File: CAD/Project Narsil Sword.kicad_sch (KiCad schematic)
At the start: 7 parts, among them SW1 SW_SPDT, U1 BAT-HLD-006-SMT, X1 Badgelife_sao_connector_v169b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, X2 Badgelife_sao_connector_v169b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, X3 Badgelife_sao_connector_v169b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, X4 Badgelife_sao_connector_v169b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, X5 Badgelife_sao_connector_v169b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

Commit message: creating schematic
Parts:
- U1: footprint BadgePirates:BatteryHolder_LINX_BAT-HLD-012-SMT -> BadgePirates:BatteryHolder_MPD_BC2003_1x2032
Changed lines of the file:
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@@
       (effects (font (size 1.27 1.27)) (justify left))
     )
-    (property "Footprint" "BadgePirates:BatteryHolder_LINX_BAT-HLD-012-SMT" (id 2) (at 106.68 85.09 0)
+    (property "Footprint" "BadgePirates:BatteryHolder_MPD_BC2003_1x2032" (id 2) (at 106.68 85.09 0)
       (effects (font (size 1.27 1.27)) (justify left) hide)
     )
@@
     )
     (path "/1e97e274-03d3-49f2-965f-f4108456c327"
-      (reference "U1") (unit 1) (value "BAT-HLD-006-SMT") (footprint "BadgePirates:BatteryHolder_LINX_BAT-HLD-012-SMT")
+      (reference "U1") (unit 1) (value "BAT-HLD-006-SMT") (footprint "BadgePirates:BatteryHolder_MPD_BC2003_1x2032")
     )
     (path "/06e1571b-569f-4df7-9572-da619078c70c"

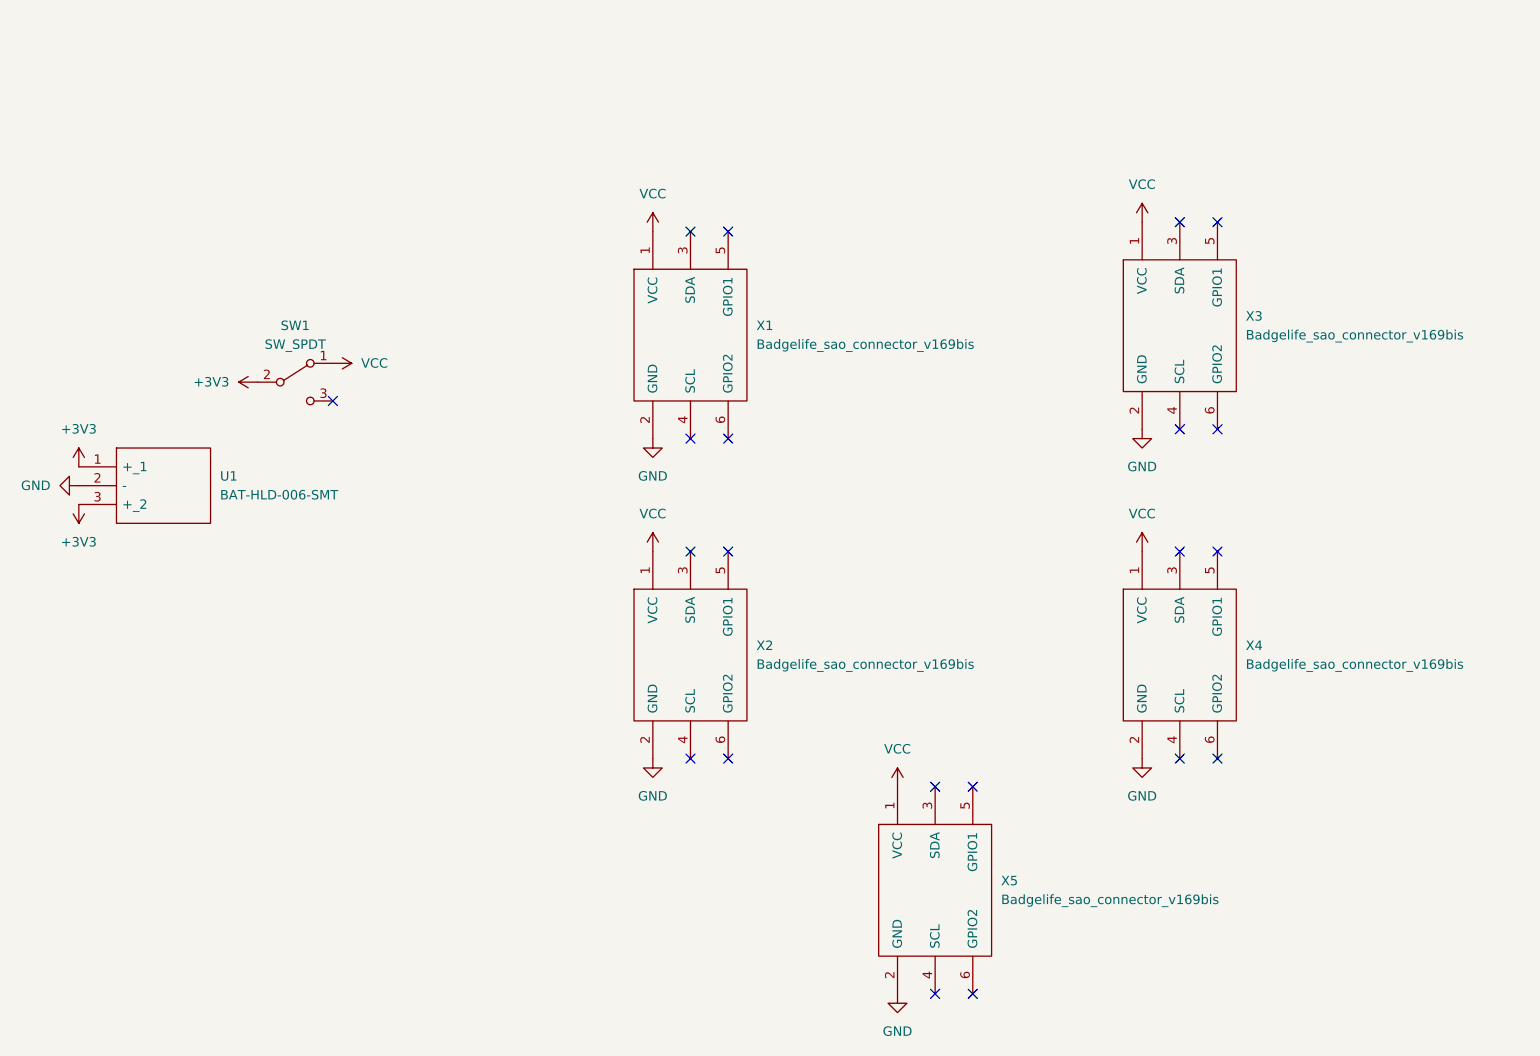
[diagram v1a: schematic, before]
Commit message: update Battery Footprint
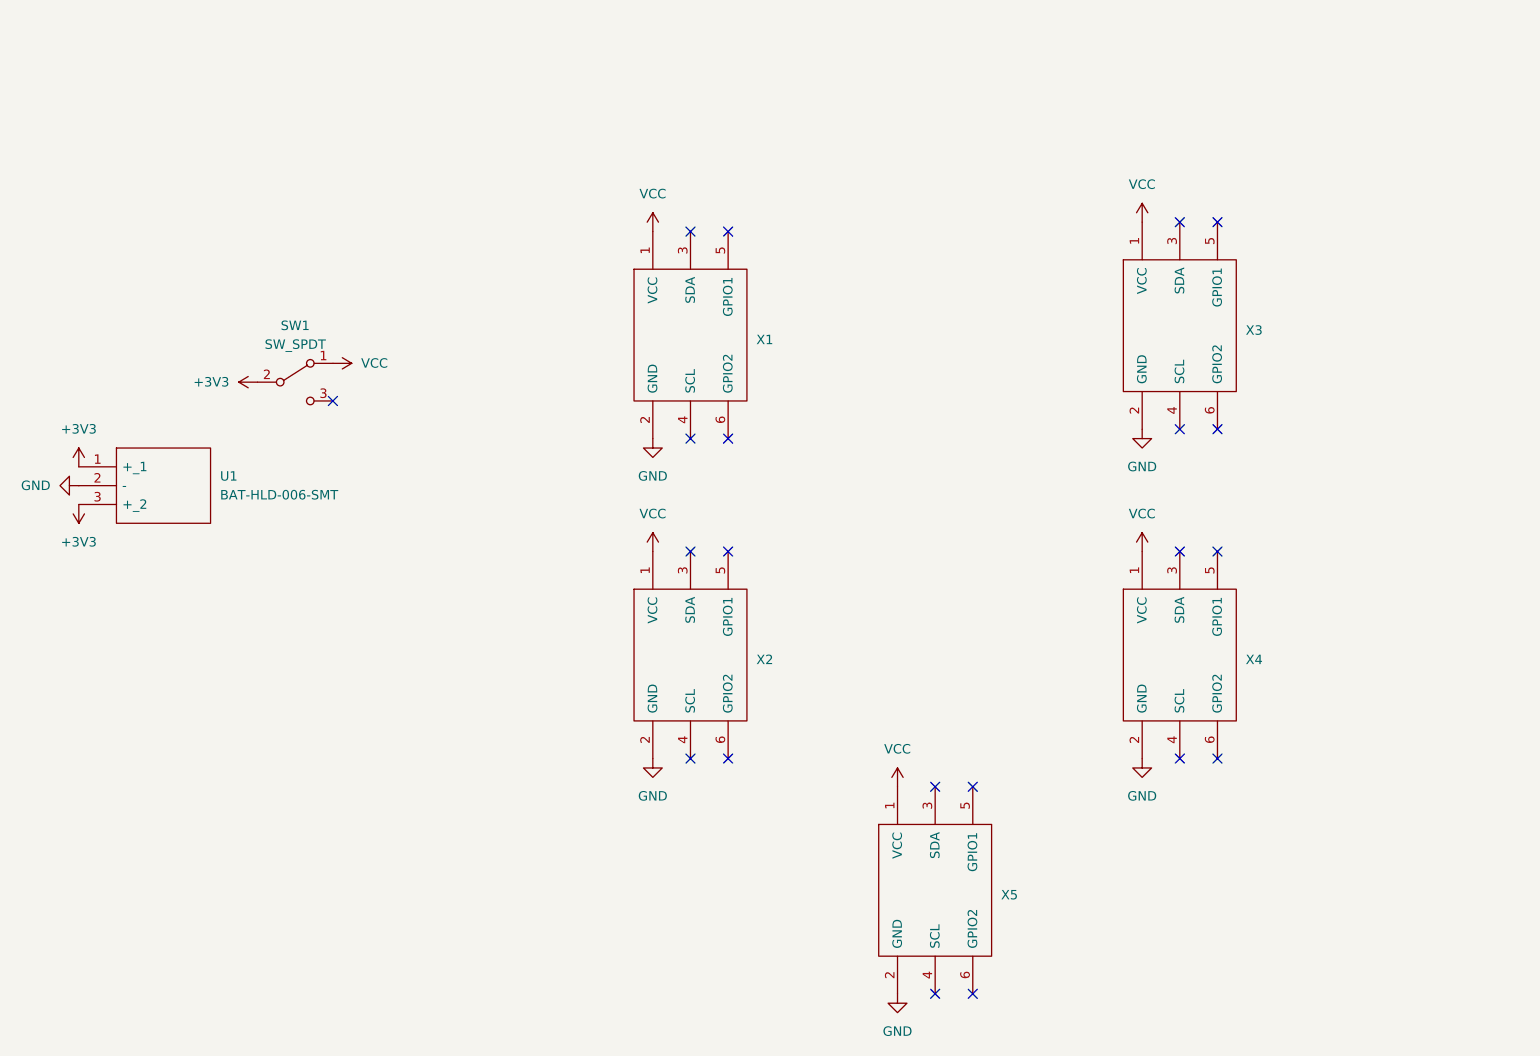
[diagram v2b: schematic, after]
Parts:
- U1: footprint BadgePirates:BatteryHolder_MPD_BC2003_1x2032 -> BadgePirates:BatteryHolder_MPD_BC2003_1x2032_Fixed
- X1, X2, X3, X4, X5: value Badgelife_sao_connector_v169bis -> sao

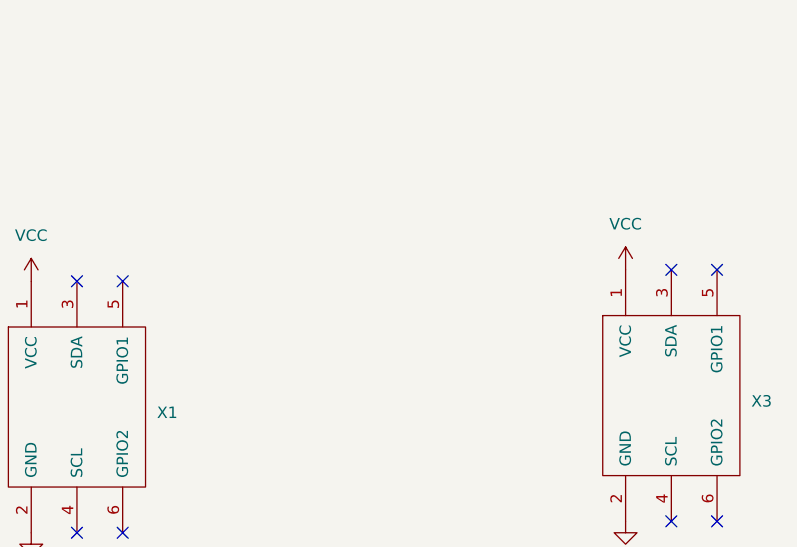
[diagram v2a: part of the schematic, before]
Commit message: update with fixes, resize and Bigger battery
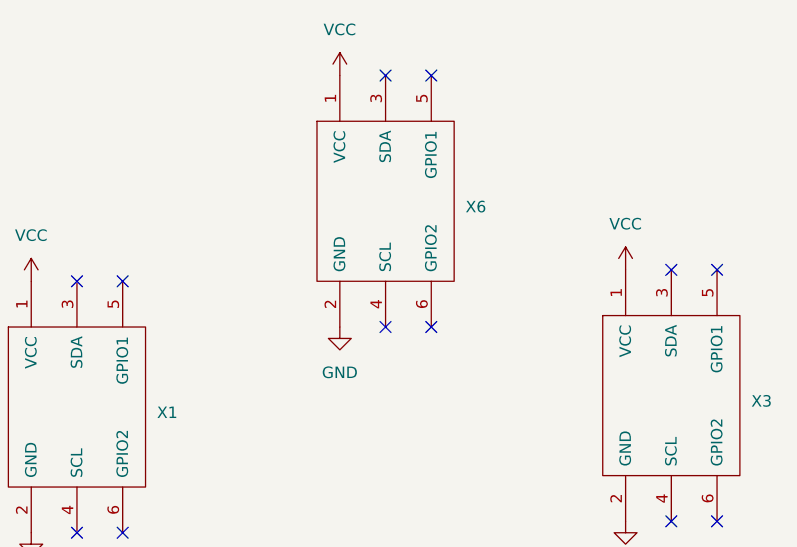
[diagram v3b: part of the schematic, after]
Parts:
- added X6: sao, BadgePirates:Badgelife-SAOv169-SAO_Side_B.SLK, symbol BadgePirates:Badgelife_sao_connector_v169bis
- U1: footprint BadgePirates:BatteryHolder_MPD_BC2003_1x2032_Fixed -> BadgePirates:BATHLD006SMT - CR2450
- X1, X2, X3, X4, X5: footprint BadgePirates:Badgelife-SAOv169-BADGE-2x3_Back -> BadgePirates:Badgelife-SAOv169-SAO_Side_B.SLK
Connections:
- net GND: now also X6.2 (GND)
- net VCC: now also X6.1 (VCC)
- no-connect marks 21 -> 25
